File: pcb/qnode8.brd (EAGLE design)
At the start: 50 x 22.4 mm, 65 parts, among them IC1 STM32F401CCU6, IC2 S25FL064K, IC3 LM3671MF-ADJ, IC4 AX5243, IC5 MCP73831-2ATI/OT, X1 BU-SMA-G, X2 USB-MICROB

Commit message: Finish schematic and board layout
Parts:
- removed LED2: (no value), led:LED3MM
- removed SWGND: (no value), wirepad:5-1,8
- removed U$1, U$2: XTAL-7M, qyx-misc:XTAL_7M
- added ANT: BU-SMA-G, con-coax:BU-SMA-G
- added C20: 10nF, rcl:C0603
- added GND: TPB2,54, testpad:B2,54
- added L2: FB, rcl:L2012C
- added R8: 470R, rcl:R0603
- added ST: (no value), led:LED3MM
- added USB: USB-MICROB, SparkFun:USB-MICROB
- BAT: value (none) -> 332-02; device SparkFun:MOLEX-1X2 -> con-garry:332-02
- RX, SWCLK, SWDIO, TX, VBAT: value (none) -> TPB2,54; device wirepad:5-1,8 -> testpad:B2,54
- X1: value BU-SMA-G -> XTAL-7M; device con-coax:BU-SMA-G -> qyx-misc:XTAL_7M
- X2: value USB-MICROB -> XTAL-7M; device SparkFun:USB-MICROB -> qyx-misc:XTAL_7M
- moved X1 36.5 mm to (9.60, 17.4), flipped to the top, turned to 270 degrees
- moved X2 27.4 mm to (28.6, 10.8), turned to 180 degrees
- moved VBAT 12.1 mm to (6.20, 3.00), turned to 180 degrees
- moved C15 4.44 mm to (33.4, 7.00), turned to 0 degrees
- moved R5 4.28 mm to (35.6, 10.0)
- moved SWCLK 3.62 mm to (19.4, 17.8)
- moved C14 2.97 mm to (29.8, 5.80)
- moved SWDIO 2.72 mm to (19.4, 15.0)
- moved IC5 2.24 mm to (32.6, 3.40)
- moved R7 2.01 mm to (35.0, 3.80)
- moved R2 1.56 mm to (11.2, 8.20), turned to 0 degrees
- moved RX 1.28 mm to (10.0, 15.0)
- moved BAT 1.08 mm to (45.4, 4.20), turned to 270 degrees
- moved TX 0.89 mm to (12.8, 15.0)
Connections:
- removed net LED_STAT: IC1.13
- new net BTN1: IC1.10, S1.2
- new net LED1: IC1.11, R8.2
- new net N$23: R8.1, ST.K
- new net N$24: C20.1, L2.1, USB.VBUS
- net +3V3: now also S1.1, ST.A
- net CHG_STAT: now also IC1.20
- net CON_RX: now also RX.TP; no longer RX.1
- net CON_TX: now also TX.TP; no longer TX.1
- net GND: now also ANT.2, ANT.3, ANT.4, ANT.5, BAT.2, C20.2, GND.TP, USB.GND, X2.2, X2.4; no longer BAT.1, SWGND.1, U$1.2, U$1.4, U$2.2, U$2.4, X1.3, X1.5, X2.GND
- net N$14: now also ANT.1; no longer X1.1
- net N$20: now also X2.3; no longer U$2.3
- net N$21: now also X2.1; no longer U$2.1
- net N$8: now also X1.1; no longer U$1.1
- net N$9: now also X1.3; no longer U$1.3
- net SWCLK: now also SWCLK.TP; no longer SWCLK.1
- net SWDIO: now also SWDIO.TP; no longer SWDIO.1
- net USB_DM: now also USB.D-; no longer X2.D-
- net USB_DP: now also USB.D+; no longer X2.D+
- net VBAT: now also BAT.1, VBAT.TP; no longer BAT.2, VBAT.1
- net VUSB: now also L2.2; no longer X2.VBUS
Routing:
- net +3V3: track 17.8 -> 61.3 mm, vias 0 -> 7
- net N$24: track 0.00 -> 36.6 mm
- net VUSB: track 36.0 -> 4.34 mm
- net CHG_STAT: track 0.00 -> 23.8 mm, vias 0 -> 2
- net VBAT_SENSE: track 4.37 -> 24.1 mm, vias 0 -> 2
- net VBAT: track 41.8 -> 60.3 mm, vias 1 -> 4
- net BTN1: track 0.00 -> 17.4 mm, vias 0 -> 2
- net USB_DP: track 13.5 -> 26.2 mm, vias 0 -> 2
- net USB_DM: track 13.1 -> 24.3 mm, vias 0 -> 2
- net LED1: track 0.00 -> 9.23 mm, vias 0 -> 2
- net GND: track 3.87 -> 11.7 mm, vias 82 -> 95
- net N$23: track 0.00 -> 5.23 mm
- net SWCLK: track 6.21 -> 2.70 mm
- net CON_TX: track 9.04 -> 8.05 mm
- net CON_RX: track 10.1 -> 9.52 mm
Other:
- board text added: "CC-BY-SA qyx@krtko.org"
- board text added: "qNode8-1.0.0+20160811"

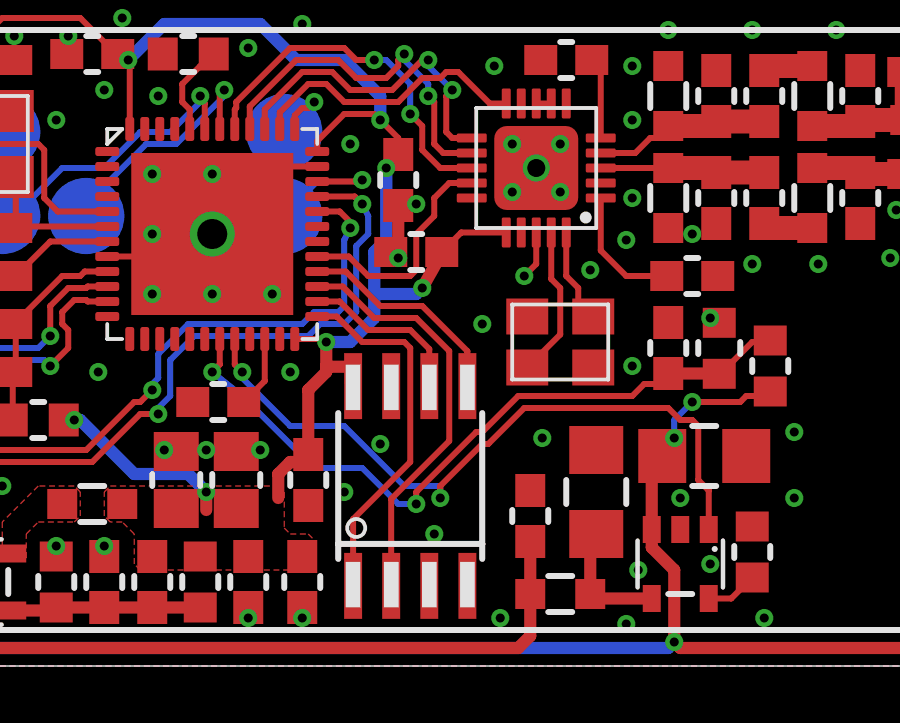
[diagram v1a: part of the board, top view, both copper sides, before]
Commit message: Fix unconnected USB_VBUS
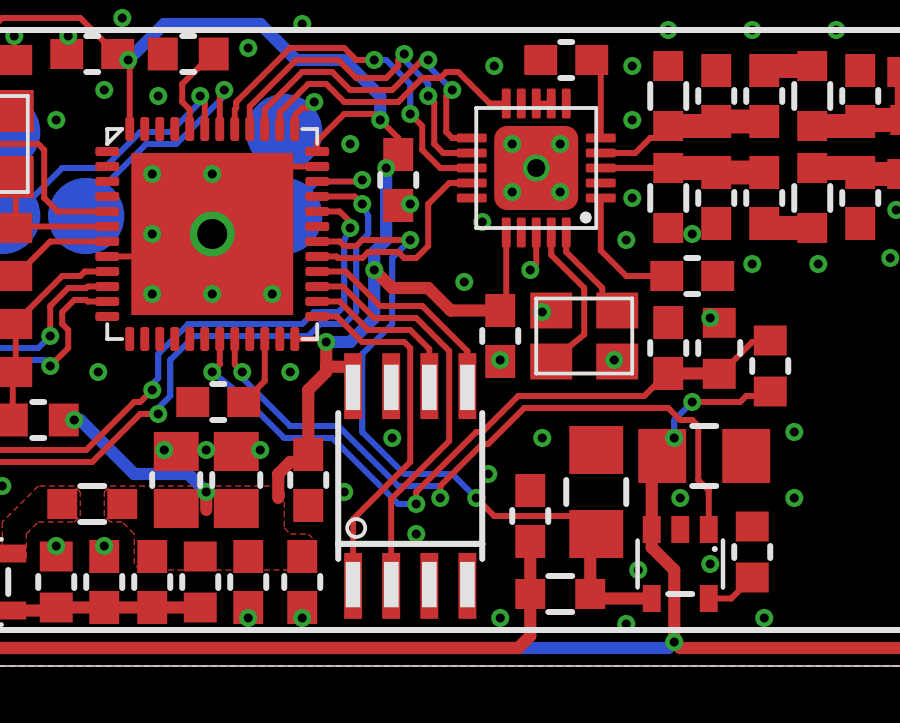
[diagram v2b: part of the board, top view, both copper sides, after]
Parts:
- moved C4 3.96 mm to (26.6, 11.0), turned to 270 degrees
- moved X2 0.82 mm to (29.4, 11.0)
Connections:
- net N$24 renamed USB_VBUS
- net VUSB: now also IC1.30
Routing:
- net VUSB: track 4.34 -> 23.9 mm, vias 0 -> 2
- net GND: track 11.7 -> 9.27 mm, vias 95 -> 97
- net +3V3: track 61.3 -> 63.3 mm
- net RADIO_IRQ: track 7.76 -> 7.19 mm
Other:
- board text added: "qNode8-1.0.1+20160812"
- board text removed: "qNode8-1.0.0+20160811"
